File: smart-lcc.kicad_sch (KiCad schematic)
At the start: 116 parts, among them J1 280372-1, J2 F0503-ZV-24-20T-R, J3 Conn_01x24, J4 BM04B-SRSS-TB(LF)(SN), J5 BM04B-SRSS-TB(LF)(SN), J6 Micro_SD_Card_Det2, J7 Conn_01x12, J8 BM04B-SRSS-TB(LF)(SN), Q1 2N7002, Q2 2N7002, Q3 2N7002, Q4 2N7002, Q5 2N7002, SW1 SW_Push, SW2 SW_Push, U1 LM5050-1, U2 RP2040, U3 ESP32-S3-WROOM-1, U4 W25Q16JVSNIQ (Program Flash), U5 W25Q16JVSNIQ (Opt. Settings f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, U6 TPS82130, U7 74LVC1G125, U8 LM5050-1, Y1 XYDBPCNANF-12MHZ

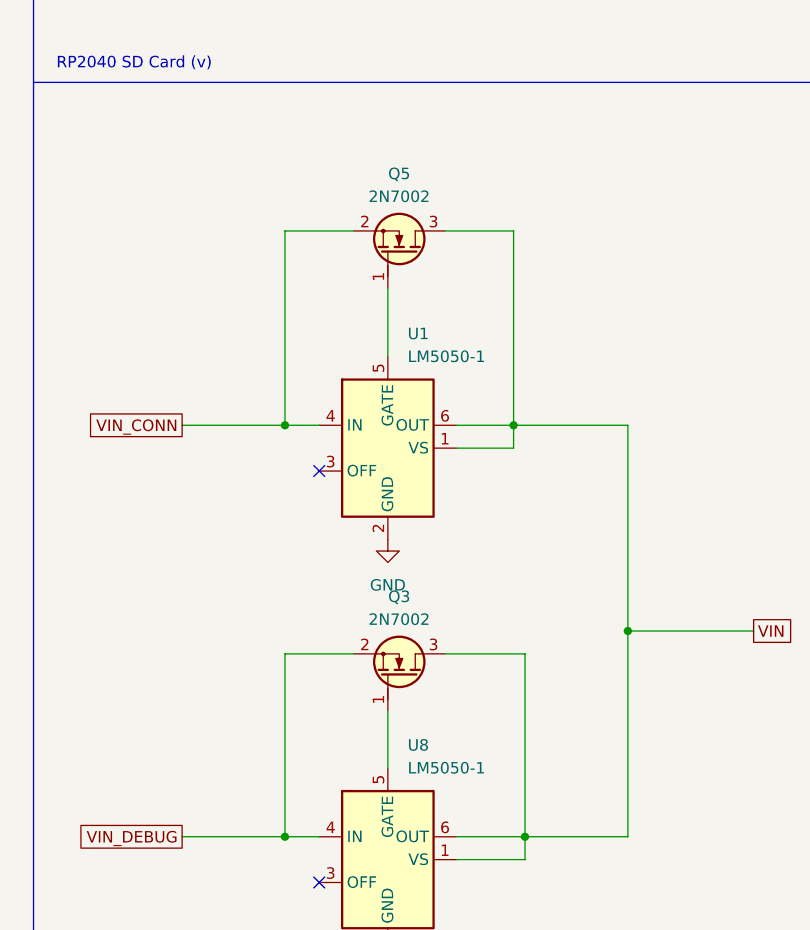
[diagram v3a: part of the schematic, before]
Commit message: Updated design for easier manufacturability
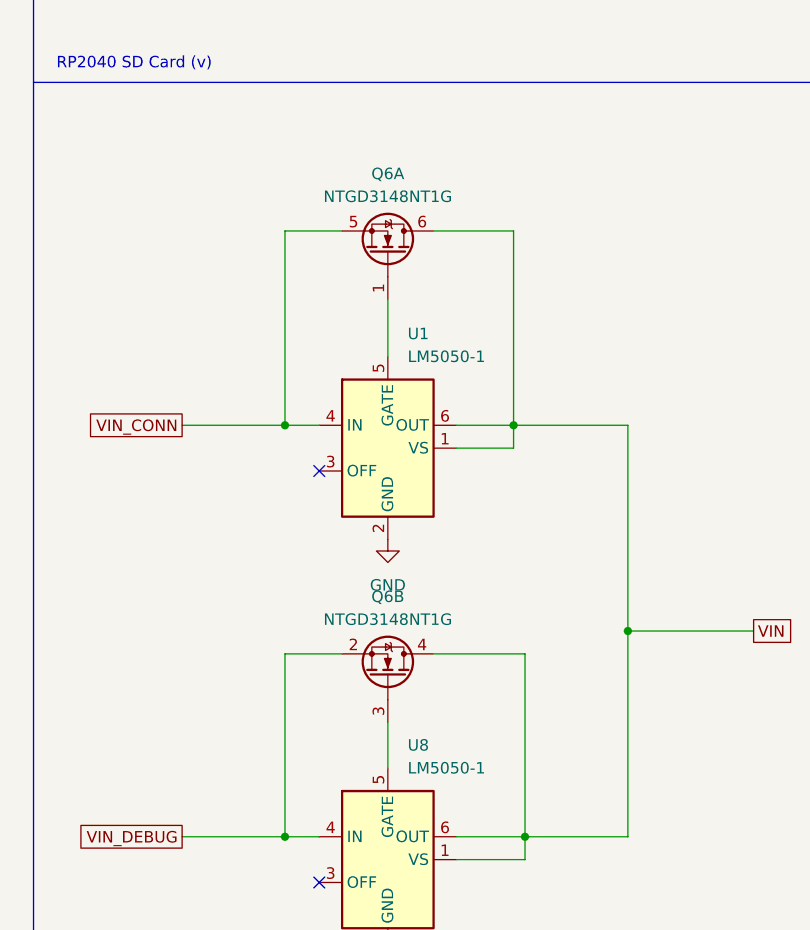
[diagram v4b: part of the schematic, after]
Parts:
- removed Q3, Q5: 2N7002, Package_TO_SOT_SMD:SOT-23, symbol PCM_Transistor_MOSFET_AKL:2N7002
- added Q6: NTGD3148NT1G, Package_SO:TSOP-6_1.65x3.05mm_P0.95mm, symbol Device:Q_Dual_NMOS_G1S2G2D2S1D1
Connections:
- net 12V_OLED: now also Q6.5 (S)
- net VIN: now also Q6.4 (D), Q6.6 (D)
- net VIN_DEBUG: now also Q6.2 (S)
- net at U8.5 (GATE): now also Q6.3 (G)
- net at U1.5 (GATE): now also Q6.1 (G)
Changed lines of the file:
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@@
     (stroke (width 0) (type default))
   )
+  (wire (pts (xy 459.74 307.34) (xy 466.09 307.34))
+    (stroke (width 0) (type default))
+  )
   (wire (pts (xy 49.53 306.07) (xy 49.53 308.61))
     (stroke (width 0) (type default))
@@
     (stroke (width 0) (type default))
   )
-  (wire (pts (xy 486.41 307.34) (xy 477.52 307.34))
-    (stroke (width 0) (type default))
-  )
   (wire (pts (xy 63.5 149.86) (xy 63.5 151.13))
     (stroke (width 0) (type default))
@@
     (stroke (width 0) (type default))
   )
+  (wire (pts (xy 471.17 314.96) (xy 471.17 320.04))
+    (stroke (width 0) (type default))
+  )
   (wire (pts (xy 166.37 222.25) (xy 166.37 210.82))
     (stroke (width 0) (type default))
@@
     (stroke (width 0) (type default))
   )
+  (wire (pts (xy 459.74 260.35) (xy 466.09 260.35))
+    (stroke (width 0) (type default))
+  )
   (wire (pts (xy 50.8 172.72) (xy 50.8 161.29))
     (stroke (width 0) (type default))
@@
     (stroke (width 0) (type default))
   )
+  (wire (pts (xy 471.17 267.97) (xy 471.17 274.32))
+    (stroke (width 0) (type default))
+  )
   (wire (pts (xy 129.54 309.88) (xy 129.54 308.61))
     (stroke (width 0) (type default))
@@
     (stroke (width 0) (type default))
   )
+  (wire (pts (xy 476.25 307.34) (xy 486.41 307.34))
+    (stroke (width 0) (type default))
+  )
   (wire (pts (xy 125.73 162.56) (xy 125.73 167.64))
     (stroke (width 0) (type default))
@@
     (stroke (width 0) (type default))
   )
-  (wire (pts (xy 467.36 307.34) (xy 459.74 307.34))
-    (stroke (width 0) (type default))
-  )
   (wire (pts (xy 27.94 161.29) (xy 27.94 149.86))
     (stroke (width 0) (type default))
@@
     (stroke (width 0) (type default))
   )
+  (wire (pts (xy 476.25 260.35) (xy 485.14 260.35))
+    (stroke (width 0) (type default))
+  )
   (wire (pts (xy 80.01 154.94) (xy 80.01 161.29))
     (stroke (width 0) (type default))
@@
     (stroke (width 0) (type default))
   )
-  (wire (pts (xy 467.36 260.35) (xy 459.74 260.35))
-    (stroke (width 0) (type default))
-  )
   (wire (pts (xy 520.7 36.83) (xy 520.7 45.72))
     (stroke (width 0) (type default))
@@
     (stroke (width 0) (type default))
   )
-  (wire (pts (xy 471.17 266.7) (xy 471.17 274.32))
-    (stroke (width 0) (type default))
-  )
   (wire (pts (xy 187.96 100.33) (xy 203.2 100.33))
     (stroke (width 0) (type default))
@@
     (stroke (width 0) (type default))
   )
-  (wire (pts (xy 485.14 260.35) (xy 477.52 260.35))
-    (stroke (width 0) (type default))
-  )
   (wire (pts (xy 15.24 161.29) (xy 15.24 149.86))
     (stroke (width 0) (type default))
@@
     (stroke (width 0) (type default))
   )
-  (wire (pts (xy 471.17 313.69) (xy 471.17 320.04))
-    (stroke (width 0) (type default))
-  )
   (polyline (pts (xy 247.65 212.09) (xy 431.8 212.09))
     (stroke (width 0) (type default))
@@
     )
   )
+  (symbol (lib_id "Device:Q_Dual_NMOS_G1S2G2D2S1D1") (at 471.17 309.88 270) (mirror x) (unit 2)
+    (in_bom yes) (on_board yes) (dnp no)
+    (property "Reference" "Q6" (at 471.17 300.99 90)
+      (effects (font (size 1.27 1.27)))
+    )
+    (property "Value" "NTGD3148NT1G" (at 471.17 303.53 90)
+      (effects (font (size 1.27 1.27)))
+    )
+    (property "Footprint" "Package_SO:TSOP-6_1.65x3.05mm_P0.95mm" (at 471.17 304.8 0)
+      (effects (font (size 1.27 1.27)) hide)
+    )
+    (property "Datasheet" "~" (at 471.17 304.8 0)
+      (effects (font (size 1.27 1.27)) hide)
+    )
+    (property "LCSC" "C77713" (at 471.17 309.88 90)
+      (effects (font (size 1.27 1.27)) hide)
+    )
+    (pin "1")
+    (pin "5")
+    (pin "6")
+    (pin "2")
+    (pin "3")
+    (pin "4")
+    (instances
+      (project "smart-lcc"
+        (path "/8090f672-69d7-45b0-9be9-e805048b83ac"
+          (reference "Q6") (unit 2)
+        )
+      )
+    )
+  )
   (symbol (lib_id "Device:C_Small") (at 113.03 303.53 180) (unit 1)
     (in_bom yes) (on_board yes) (dnp no) (fields_autoplaced)
@@
     )
   )
+  (symbol (lib_id "Device:Q_Dual_NMOS_G1S2G2D2S1D1") (at 471.17 262.89 270) (mirror x) (unit 1)
+    (in_bom yes) (on_board yes) (dnp no)
+    (property "Reference" "Q6" (at 471.17 254 90)
+      (effects (font (size 1.27 1.27)))
+    )
+    (property "Value" "NTGD3148NT1G" (at 471.17 256.54 90)
+      (effects (font (size 1.27 1.27)))
+    )
+    (property "Footprint" "Package_SO:TSOP-6_1.65x3.05mm_P0.95mm" (at 471.17 257.81 0)
+      (effects (font (size 1.27 1.27)) hide)
+    )
+    (property "Datasheet" "~" (at 471.17 257.81 0)
+      (effects (font (size 1.27 1.27)) hide)
+    )
+    (property "LCSC" "C77713" (at 471.17 262.89 90)
+      (effects (font (size 1.27 1.27)) hide)
+    )
+    (pin "1")
+    (pin "5")
+    (pin "6")
+    (pin "2")
+    (pin "3")
+    (pin "4")
+    (instances
+      (project "smart-lcc"
+        (path "/8090f672-69d7-45b0-9be9-e805048b83ac"
+          (reference "Q6") (unit 1)
+        )
+      )
+    )
+  )
   (symbol (lib_id "Device:C_Small") (at 347.98 48.26 90) (unit 1)
     (in_bom yes) (on_board yes) (dnp no)
@@
     )
   )
-  (symbol (lib_id "PCM_Transistor_MOSFET_AKL:2N7002") (at 472.44 309.88 270) (mirror x) (unit 1)
-    (in_bom yes) (on_board yes) (dnp no)
-    (property "Reference" "Q3" (at 472.44 300.99 90)
-      (effects (font (size 1.27 1.27)))
-    )
-    (property "Value" "2N7002" (at 472.44 303.53 90)
-      (effects (font (size 1.27 1.27)))
-    )
-    (property "Footprint" "Package_TO_SOT_SMD:SOT-23" (at 474.98 304.8 0)
-      (effects (font (size 1.27 1.27)) hide)
-    )
-    (property "Datasheet" "https://www.tme.eu/Document/7df5cae36abdfcedddb681f5be886f05/2N7000.pdf" (at 472.44 309.88 0)
-      (effects (font (size 1.27 1.27)) hide)
-    )
-    (property "JLCPCB Basic" "Y" (at 472.44 309.88 0)
-      (effects (font (size 1.27 1.27)) hide)
-    )
-    (property "LCSC" "C8545" (at 472.44 309.88 0)
-      (effects (font (size 1.27 1.27)) hide)
-    )
-    (pin "1")
-    (pin "2")
-    (pin "3")
-    (instances
-      (project "smart-lcc"
-        (path "/8090f672-69d7-45b0-9be9-e805048b83ac"
-          (reference "Q3") (unit 1)
-        )
-      )
-    )
-  )
   (symbol (lib_id "power:GND") (at 73.66 242.57 270) (unit 1)
     (in_bom yes) (on_board yes) (dnp no) (fields_autoplaced)
@@
         )
       )
-    )
-  )
-  (symbol (lib_id "PCM_Transistor_MOSFET_AKL:2N7002") (at 472.44 262.89 270) (mirror x) (unit 1)
-    (in_bom yes) (on_board yes) (dnp no)
-    (property "Reference" "Q5" (at 472.44 254 90)
-      (effects (font (size 1.27 1.27)))
-    )
-    (property "Value" "2N7002" (at 472.44 256.54 90)
-      (effects (font (size 1.27 1.27)))
-    )
-    (property "Footprint" "Package_TO_SOT_SMD:SOT-23" (at 474.98 257.81 0)
-      (effects (font (size 1.27 1.27)) hide)
-    )
-    (property "Datasheet" "https://www.tme.eu/Document/7df5cae36abdfcedddb681f5be886f05/2N7000.pdf" (at 472.44 262.89 0)
-      (effects (font (size 1.27 1.27)) hide)
-    )
-    (property "JLCPCB Basic" "Y" (at 472.44 262.89 0)
-      (effects (font (size 1.27 1.27)) hide)
-    )
-    (property "LCSC" "C8545" (at 472.44 262.89 0)
-      (effects (font (size 1.27 1.27)) hide)
-    )
-    (pin "1")
-    (pin "2")
-    (pin "3")
-    (instances
-      (project "smart-lcc"
-        (path "/8090f672-69d7-45b0-9be9-e805048b83ac"
-          (reference "Q5") (unit 1)
-        )
-      )

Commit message: Added revision R2C
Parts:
- added R26, R27: 18K7, Resistor_SMD:R_0402_1005Metric, symbol Device:R_Small
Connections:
- net 12V_OLED: now also R26.1
- net GND: now also R26.2, R27.2
- net VIN_DEBUG: now also R27.1
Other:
- note added: "Because GPIO35-37 are NC:ed, this design can also use ESP32-S3-WROOM-2U, if that ever gets released."
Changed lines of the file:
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@@
   (junction (at 66.04 151.13) (diameter 0) (color 0 0 0 0)
   )
+  (junction (at 452.12 281.94) (diameter 0) (color 0 0 0 0)
+  )
   (junction (at 350.52 53.34) (diameter 0) (color 0 0 0 0)
   )
@@
   (junction (at 129.54 308.61) (diameter 0) (color 0 0 0 0)
   )
+  (junction (at 453.39 327.66) (diameter 0) (color 0 0 0 0)
+  )
   (junction (at 58.42 151.13) (diameter 0) (color 0 0 0 0)
   )
@@
     (stroke (width 0) (type default))
   )
+  (wire (pts (xy 452.12 281.94) (xy 459.74 281.94))
+    (stroke (width 0) (type default))
+  )
   (wire (pts (xy 69.85 245.11) (xy 73.66 245.11))
     (stroke (width 0) (type default))
@@
     (stroke (width 0) (type default))
   )
+  (wire (pts (xy 452.12 281.94) (xy 452.12 287.02))
+    (stroke (width 0) (type default))
+  )
   (wire (pts (xy 346.71 331.47) (xy 374.65 331.47))
     (stroke (width 0) (type default))
@@
     (stroke (width 0) (type default))
   )
-  (wire (pts (xy 448.31 281.94) (xy 459.74 281.94))
+  (wire (pts (xy 448.31 281.94) (xy 452.12 281.94))
     (stroke (width 0) (type default))
   )
@@
     (stroke (width 0) (type default))
   )
+  (wire (pts (xy 452.12 292.1) (xy 452.12 297.18))
+    (stroke (width 0) (type default))
+  )
   (wire (pts (xy 50.8 213.36) (xy 50.8 214.63))
     (stroke (width 0) (type default))
@@
     (stroke (width 0) (type default))
   )
-  (wire (pts (xy 448.31 327.66) (xy 459.74 327.66))
+  (wire (pts (xy 448.31 327.66) (xy 453.39 327.66))
+    (stroke (width 0) (type default))
+  )
+  (wire (pts (xy 453.39 327.66) (xy 453.39 334.01))
     (stroke (width 0) (type default))
   )
@@
     (stroke (width 0) (type default))
   )
+  (wire (pts (xy 453.39 339.09) (xy 453.39 344.17))
+    (stroke (width 0) (type default))
+  )
   (polyline (pts (xy 431.8 212.09) (xy 431.8 243.84))
     (stroke (width 0) (type default))
@@
     (stroke (width 0) (type default))
   )
+  (wire (pts (xy 453.39 327.66) (xy 459.74 327.66))
+    (stroke (width 0) (type default))
+  )
   (wire (pts (xy 15.24 161.29) (xy 15.24 149.86))
     (stroke (width 0) (type default))
@@
     (effects (font (size 1.27 1.27)) (justify left bottom))
   )
+  (text "Because GPIO35-37 are NC:ed,\nthis design can also use \nESP32-S3-WROOM-2U, if that\never gets released."
+    (at 220.98 331.47 0)
+    (effects (font (size 1.27 1.27)) (justify left bottom))
+  )
   (text "Debug daughter board connector (v)" (at 13.97 195.58 0)
     (effects (font (size 1.27 1.27)) (justify left bottom))
@@
     )
   )
+  (symbol (lib_id "power:GND") (at 453.39 344.17 0) (unit 1)
+    (in_bom yes) (on_board yes) (dnp no) (fields_autoplaced)
+    (property "Reference" "#PWR0102" (at 453.39 350.52 0)
+      (effects (font (size 1.27 1.27)) hide)
+    )
+    (property "Value" "GND" (at 453.39 349.25 0)
+      (effects (font (size 1.27 1.27)))
+    )
+    (property "Footprint" "" (at 453.39 344.17 0)
+      (effects (font (size 1.27 1.27)) hide)
+    )
+    (property "Datasheet" "" (at 453.39 344.17 0)
+      (effects (font (size 1.27 1.27)) hide)
+    )
+    (pin "1")
+    (instances
+      (project "smart-lcc"
+        (path "/8090f672-69d7-45b0-9be9-e805048b83ac"
+          (reference "#PWR0102") (unit 1)
+        )
+      )
+    )
+  )
   (symbol (lib_id "Device:R") (at 187.96 93.98 180) (unit 1)
     (in_bom yes) (on_board yes) (dnp no) (fields_autoplaced)
@@
     )
   )
+  (symbol (lib_id "Device:R_Small") (at 453.39 336.55 0) (unit 1)
+    (in_bom yes) (on_board yes) (dnp no) (fields_autoplaced)
+    (property "Reference" "R27" (at 455.93 335.28 0)
+      (effects (font (size 1.27 1.27)) (justify left))
+    )
+    (property "Value" "18K7" (at 455.93 337.82 0)
+      (effects (font (size 1.27 1.27)) (justify left))
+    )
+    (property "Footprint" "Resistor_SMD:R_0402_1005Metric" (at 453.39 336.55 0)
+      (effects (font (size 1.27 1.27)) hide)
+    )
+    (property "Datasheet" "~" (at 453.39 336.55 0)
+      (effects (font (size 1.27 1.27)) hide)
+    )
+    (property "LCSC" "C102855" (at 453.39 336.55 0)
+      (effects (font (size 1.27 1.27)) hide)
+    )
+    (pin "1")
+    (pin "2")
+    (instances
+      (project "smart-lcc"
+        (path "/8090f672-69d7-45b0-9be9-e805048b83ac"
+          (reference "R27") (unit 1)
+        )
+      )
+    )
+  )
   (symbol (lib_id "Connector:TestPoint_Small") (at 69.85 247.65 0) (unit 1)
     (in_bom no) (on_board yes) (dnp no) (fields_autoplaced)
@@
     )
   )
+  (symbol (lib_id "Device:R_Small") (at 452.12 289.56 0) (unit 1)
+    (in_bom yes) (on_board yes) (dnp no) (fields_autoplaced)
+    (property "Reference" "R26" (at 454.66 288.29 0)
+      (effects (font (size 1.27 1.27)) (justify left))
+    )
+    (property "Value" "18K7" (at 454.66 290.83 0)
+      (effects (font (size 1.27 1.27)) (justify left))
+    )
+    (property "Footprint" "Resistor_SMD:R_0402_1005Metric" (at 452.12 289.56 0)
+      (effects (font (size 1.27 1.27)) hide)
+    )
+    (property "Datasheet" "~" (at 452.12 289.56 0)
+      (effects (font (size 1.27 1.27)) hide)
+    )
+    (property "LCSC" "C102855" (at 452.12 289.56 0)
+      (effects (font (size 1.27 1.27)) hide)
+    )
+    (pin "1")
+    (pin "2")
+    (instances
+      (project "smart-lcc"
+        (path "/8090f672-69d7-45b0-9be9-e805048b83ac"
+          (reference "R26") (unit 1)
+        )
+      )
+    )
+  )
   (symbol (lib_id "power:+3V3") (at 125.73 162.56 0) (unit 1)
     (in_bom yes) (on_board yes) (dnp no) (fields_autoplaced)
@@
         )
       )
+    )
+  )
+  (symbol (lib_id "power:GND") (at 452.12 297.18 0) (unit 1)
+    (in_bom yes) (on_board yes) (dnp no) (fields_autoplaced)
+    (property "Reference" "#PWR091" (at 452.12 303.53 0)
+      (effects (font (size 1.27 1.27)) hide)
+    )
+    (property "Value" "GND" (at 452.12 302.26 0)
+      (effects (font (size 1.27 1.27)))
+    )
+    (property "Footprint" "" (at 452.12 297.18 0)
+      (effects (font (size 1.27 1.27)) hide)
+    )
+    (property "Datasheet" "" (at 452.12 297.18 0)
+      (effects (font (size 1.27 1.27)) hide)
+    )
+    (pin "1")
+    (instances
+      (project "smart-lcc"
+        (path "/8090f672-69d7-45b0-9be9-e805048b83ac"
+          (reference "#PWR091") (unit 1)
+        )
+      )

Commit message: Updated to use a more flexible FPC connector footprint
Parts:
- J2: footprint 2N7002:FPC_24 -> FlexibleFPC:Flexible24Pin
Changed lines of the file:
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@@
       (effects (font (size 1.27 1.27)))
     )
-    (property "Footprint" "2N7002:FPC_24" (at 40.64 144.78 0)
+    (property "Footprint" "FlexibleFPC:Flexible24Pin" (at 40.64 144.78 0)
       (effects (font (size 1.27 1.27)) hide)
     )
